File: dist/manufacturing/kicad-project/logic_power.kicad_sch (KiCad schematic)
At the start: 59 parts, among them U22 LMR36510ADDAR, U23 LM66100DCKR, U24 LM66100DCKR, U5 LMR36510ADDAR

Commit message: Complete orderable PD1180-EPR board release
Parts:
- removed GND (x11): GND, symbol Custom:rail_down
- removed USB_VBUS (x2): USB_VBUS, symbol Custom:rail_up
- removed V3V3 (x5): V3V3, symbol Custom:rail_up
- removed V3V3_MOTOR (x5): V3V3_MOTOR, symbol Custom:rail_up
- removed V3V3_USB (x5): V3V3_USB, symbol Custom:rail_up
- removed VMOTOR (x2): VMOTOR, symbol Custom:rail_up
- added GND (x13): GND, symbol Custom:rail_down
- added USB_VBUS (x2): USB_VBUS, symbol Custom:rail_up
- added V3V3 (x4): V3V3, symbol Custom:rail_up
- added V3V3_MOTOR (x5): V3V3_MOTOR, symbol Custom:rail_up
- added V3V3_USB (x6): V3V3_USB, symbol Custom:rail_up
- added VMOTOR (x2): VMOTOR, symbol Custom:rail_up
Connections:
- net GND: now also C15.2, C16.2
- net at C70.1, U24.1 (VIN): now also V3V3_MOTOR.1
- net at C70.2: now also GND.1
- net at C66.1, C67.1: now also V3V3_MOTOR.1; no longer C68.1
- net at C66.2, C67.2: now also GND.1; no longer C68.2
- net at C62.1, C63.1: now also VMOTOR.1
- net at C62.2, C63.2, C64.2: now also GND.1
- net at U23.2 (GND), U23.5 (ST): now also GND.1
- net at R103.2: now also GND.1
- net at U24.2 (GND), U24.5 (ST): now also GND.1
- net at U24.3 (N_CE): now also V3V3.1
- net at U24.6 (VOUT): now also V3V3.1
- net at R17.2: now also GND.1
- net at C69.1: now also V3V3_USB.1; no longer U23.1 (VIN)
- net at C69.2: now also GND.1; no longer C71.2
- net at U23.6 (VOUT): now also C71.1, V3V3.1
- net at C11.2, C12.2, C13.2: now also GND.1
- net at R104.1: now also R102.1, V3V3_MOTOR.1
- net at L1.2: now also V3V3_USB.1
- net at C15.1, C16.1: now also V3V3_USB.1; no longer C17.1
- net at U5.2 (VIN), U5.3 (EN): now also USB_VBUS.1
- net at U23.3 (N_CE): now also V3V3.1
- net at R16.1: now also R18.1, V3V3_USB.1
- net at U22.2 (VIN), U22.3 (EN): now also VMOTOR.1
- net at L2.2: now also V3V3_MOTOR.1
- net at C11.1, C12.1: now also USB_VBUS.1
- new net: C68.1, V3V3_MOTOR.1
- new net: C68.2, GND.1
- new net: C17.1, V3V3_USB.1
- new net: C17.2, GND.1
- new net: C71.2, GND.1
- new net: U23.1 (VIN), V3V3_USB.1
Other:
- note added: "U5: USB 5 V buck. U22: motor-bus auxiliary buck. U23/U24: ideal-diode OR into the shared 3.3 V rail."

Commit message: Fix schematic style and top-side reset switch
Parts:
- removed GND (x13): GND, symbol Custom:rail_down
- removed USB_VBUS (x2): USB_VBUS, symbol Custom:rail_up
- removed V3V3 (x4): V3V3, symbol Custom:rail_up
- removed V3V3_MOTOR (x5): V3V3_MOTOR, symbol Custom:rail_up
- removed V3V3_USB (x6): V3V3_USB, symbol Custom:rail_up
- removed VMOTOR (x2): VMOTOR, symbol Custom:rail_up
- added GND (x14): GND, symbol Custom:rail_down
- added USB_VBUS (x2): USB_VBUS, symbol Custom:rail_up
- added V3V3 (x4): V3V3, symbol Custom:rail_up
- added V3V3_MOTOR (x5): V3V3_MOTOR, symbol Custom:rail_up
- added V3V3_USB (x6): V3V3_USB, symbol Custom:rail_up
- added VMOTOR (x2): VMOTOR, symbol Custom:rail_up
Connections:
- net GND: no longer C15.2, C16.2
- net at U24.2 (GND), U24.5 (ST): now also GND.1
- net at C70.1, U24.1 (VIN): now also V3V3_MOTOR.1
- net at U24.3 (N_CE): now also V3V3.1
- net at U24.6 (VOUT): now also V3V3.1
- net at C66.1, C67.1: now also V3V3_MOTOR.1
- net at R103.2: now also GND.1
- net at U22.2 (VIN), U22.3 (EN): now also VMOTOR.1
- net at C71.1, U23.6 (VOUT): now also V3V3.1
- net at U5.2 (VIN), U5.3 (EN): now also USB_VBUS.1
- net at C68.1: now also V3V3_MOTOR.1
- net at C68.2: now also GND.1
- net at R102.1, R104.1: now also V3V3_MOTOR.1
- net at C11.2, C12.2: now also GND.1; no longer C13.2
- net at C62.1, C63.1: now also VMOTOR.1
- net at C62.2, C63.2: now also GND.1; no longer C64.2
- net at C11.1, C12.1: now also USB_VBUS.1
- net at C69.1: now also V3V3_USB.1
- net at C69.2: now also GND.1
- net at C17.1: now also V3V3_USB.1
- net at C17.2: now also GND.1
- net at C71.2: now also GND.1
- net at L2.2: now also V3V3_MOTOR.1
- net at C15.1, C16.1: now also V3V3_USB.1
- net at R16.1, R18.1: now also V3V3_USB.1
- net at R17.2: now also GND.1
- net at L1.2: now also V3V3_USB.1
- net at U23.1 (VIN): now also V3V3_USB.1
- net at U23.2 (GND), U23.5 (ST): now also GND.1
- net at U23.3 (N_CE): now also V3V3.1
- net at C70.2: now also GND.1
- new net: C64.2, GND.1
- new net: C15.2, C16.2
- new net: C13.2, GND.1

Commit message: Use one USB-C port for PD and data
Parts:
- removed GND (x14): GND, symbol Custom:rail_down
- removed USB_VBUS (x2): USB_VBUS, symbol Custom:rail_up
- removed V3V3 (x4): V3V3, symbol Custom:rail_up
- removed V3V3_MOTOR (x5): V3V3_MOTOR, symbol Custom:rail_up
- removed V3V3_USB (x6): V3V3_USB, symbol Custom:rail_up
- removed VMOTOR (x2): VMOTOR, symbol Custom:rail_up
- added GND (x14): GND, symbol Custom:rail_down
- added USB_VBUS (x2): USB_VBUS, symbol Custom:rail_up
- added V3V3 (x4): V3V3, symbol Custom:rail_up
- added V3V3_MOTOR (x5): V3V3_MOTOR, symbol Custom:rail_up
- added V3V3_USB (x6): V3V3_USB, symbol Custom:rail_up
- added VMOTOR (x2): VMOTOR, symbol Custom:rail_up
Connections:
- net at C68.1: now also V3V3_MOTOR.1
- net at C68.2: now also GND.1
- net at C66.1, C67.1: now also V3V3_MOTOR.1
- net at U23.1 (VIN): now also V3V3_USB.1
- net at R16.1, R18.1: now also V3V3_USB.1
- net at C69.2: now also GND.1
- net at U24.2 (GND), U24.5 (ST): now also GND.1
- net at R102.1, R104.1: now also V3V3_MOTOR.1
- net at C71.1, U23.6 (VOUT): now also V3V3.1
- net at C71.2: now also GND.1
- net at R17.2: now also GND.1
- net at C17.1: now also V3V3_USB.1
- net at C17.2: now also GND.1
- net at U5.2 (VIN), U5.3 (EN): now also USB_VBUS.1
- net at L2.2: now also V3V3_MOTOR.1
- net at C64.2: now also GND.1
- net at C15.1, C16.1: now also V3V3_USB.1
- net at U22.2 (VIN), U22.3 (EN): now also VMOTOR.1
- net at L1.2: now also V3V3_USB.1
- net at C70.1, U24.1 (VIN): now also V3V3_MOTOR.1
- net at C70.2: now also GND.1
- net at R103.2: now also GND.1
- net at U23.2 (GND), U23.5 (ST): now also GND.1
- net at U23.3 (N_CE): now also V3V3.1
- net at C11.1, C12.1: now also USB_VBUS.1
- net at C11.2, C12.2: now also GND.1
- net at U24.6 (VOUT): now also V3V3.1
- net at C62.1, C63.1: now also VMOTOR.1
- net at C62.2, C63.2: now also GND.1
- net at C69.1: now also V3V3_USB.1
- net at U24.3 (N_CE): now also V3V3.1
- net at C13.2: now also GND.1

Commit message: fix: finalize single-port EPR controller
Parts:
- removed GND (x14): GND, symbol Custom:rail_down
- removed USB_VBUS (x2): USB_VBUS, symbol Custom:rail_up
- removed V3V3 (x4): V3V3, symbol Custom:rail_up
- removed V3V3_MOTOR (x5): V3V3_MOTOR, symbol Custom:rail_up
- removed V3V3_USB (x6): V3V3_USB, symbol Custom:rail_up
- removed VMOTOR (x2): VMOTOR, symbol Custom:rail_up
- added R111: 10kΩ, resistor_res0603, symbol Device:boxresistor_down
- C11, C62: footprint (none) -> capacitor_cap1206
- C12, C13, C14, C63, C64, C65, C69, C70, C71: footprint (none) -> capacitor_cap0603
- C15, C16, C17, C66, C67, C68: footprint (none) -> capacitor_cap0805
- L1, L2: footprint (none) -> SWPA6045S220MT
- R102, R103, R104, R16, R17, R18: footprint (none) -> resistor_res0603
- U22, U5: footprint (none) -> LMR36510ADDAR
- U23, U24: footprint (none) -> LM66100DCKR
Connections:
- net GND: now also C11.2, C12.2, C13.2, C15.2, C16.2, C17.2, C62.2, C63.2, C64.2, C66.2, C67.2, C68.2, C69.2, C70.2, C71.2, R103.2, R17.2, U23.2 (GND), U24.2 (GND), U24.5 (ST), U5.1 (PGND), U5.9 (PAD)
- net BUCK_SW: now reaches L1.1
- net BUCK_SW: now also C14.2, U5.8 (SW)
- net V3V3_USB: now reaches L1.2
- net V3V3_USB: now also C15.1, C16.1, C17.1, C69.1, R16.1, R18.1, U23.1 (VIN), R111.1
- net V3V3_MOTOR: now reaches R102.1, R104.1
- net V3V3_MOTOR: now also C66.1, C67.1, C68.1, C70.1, L2.2, U23.3 (N_CE), U24.1 (VIN)
- net MOTOR_BUCK_FB: now reaches R102.2, R103.1
- net MOTOR_BUCK_FB: now also U22.5 (FB)
- net BUCK_VCC: now reaches C13.1
- net BUCK_VCC: now also U5.6 (VCC)
- net VMOTOR: now reaches C62.1, C63.1
- net VMOTOR: now also U22.2 (VIN), U22.3 (EN)
- net USB_VBUS: now reaches U5.2 (VIN), U5.3 (EN)
- net USB_VBUS: now also C11.1, C12.1
- net BUCK_FB: now reaches R16.2, R17.1
- net BUCK_FB: now also U5.5 (FB)
- net MOTOR_BUCK_SW: now reaches L2.1
- net MOTOR_BUCK_SW: now also C65.2, U22.8 (SW)
- net MOTOR_LOGIC_PG: now reaches U22.4 (PG)
- net MOTOR_LOGIC_PG: now also R104.2
- net MOTOR_BUCK_VCC: now reaches U22.6 (VCC)
- net MOTOR_BUCK_VCC: now also C64.1
- net MOTOR_BUCK_BOOT: now reaches U22.7 (BOOT)
- net MOTOR_BUCK_BOOT: now also C65.1
- net V3V3: now reaches C71.1, U23.6 (VOUT)
- net V3V3: now also U24.6 (VOUT)
- net LOGIC_OR_PRIORITY: now reaches U24.3 (N_CE)
- net LOGIC_OR_PRIORITY: now also U23.5 (ST), R111.2
- net LOGIC_PG: now reaches R18.2
- net LOGIC_PG: now also U5.4 (PG)
- net BUCK_BOOT: now reaches U5.7 (BOOT)
- net BUCK_BOOT: now also C14.1
- no-connect marks 0 -> 2
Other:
- note added: "LOGIC_OR_PRIORITY"
- note added: "U5: USB 5 V buck. U22: motor-bus auxiliary buck. U23/U24 + R111: status-interlocked ideal-diode OR into the shared 3.3 V rail."
- note removed: "U5: USB 5 V buck. U22: motor-bus auxiliary buck. U23/U24: ideal-diode OR into the shared 3.3 V rail."

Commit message: Implement dual USB power/data ECO and consolidate industrial I/O
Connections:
- net USB_VBUS renamed PD_VBUS
- net V3V3_USB renamed V3V3_PD
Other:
- note added: "02 / PD and Motor Backup Supplies"
- note added: "PD VBUS starts the 3.3 V rail; the motor-bus buck retains brake-control backup after PD loss."
- note added: "U5: PD 5-48 V buck. U22: VMOTOR backup buck. U23/U24 + R111: status-interlocked ideal-diode OR into the shared 3.3 V rail."
- note removed: "02 / USB and Motor Logic Supplies"
- note removed: "Either USB or motor bus sustains 3.3 V; ideal diodes block reverse current."
- note removed: "U5: USB 5 V buck. U22: motor-bus auxiliary buck. U23/U24 + R111: status-interlocked ideal-diode OR into the shared 3.3 V rail."

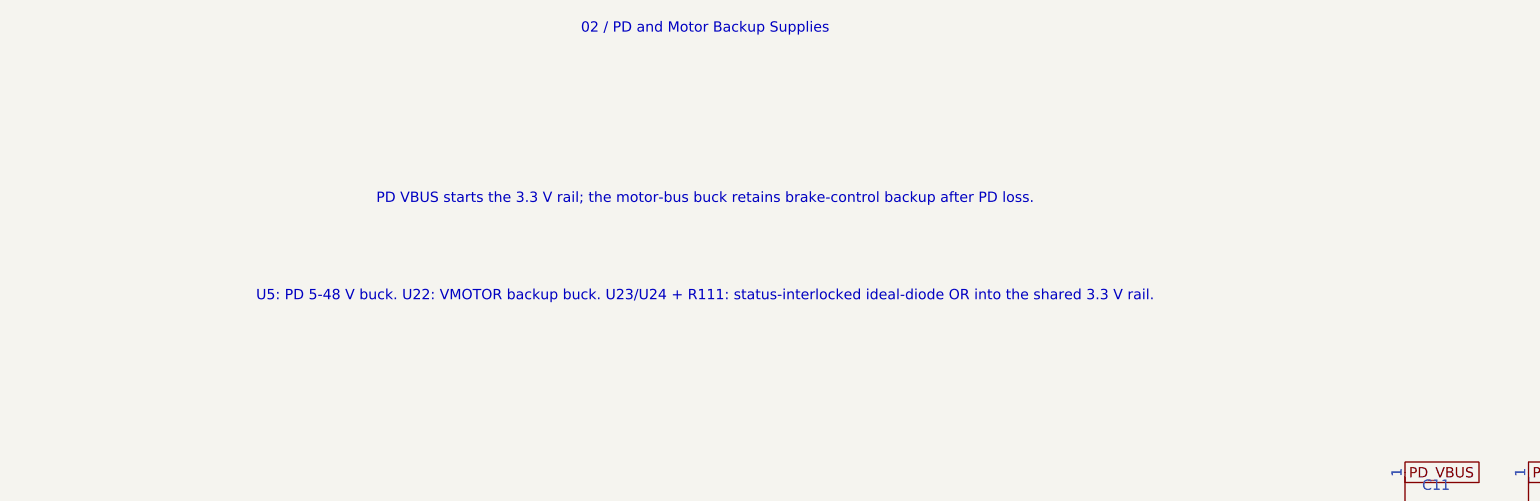
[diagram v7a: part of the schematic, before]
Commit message: Complete top-side routing and verify reference-board ECO
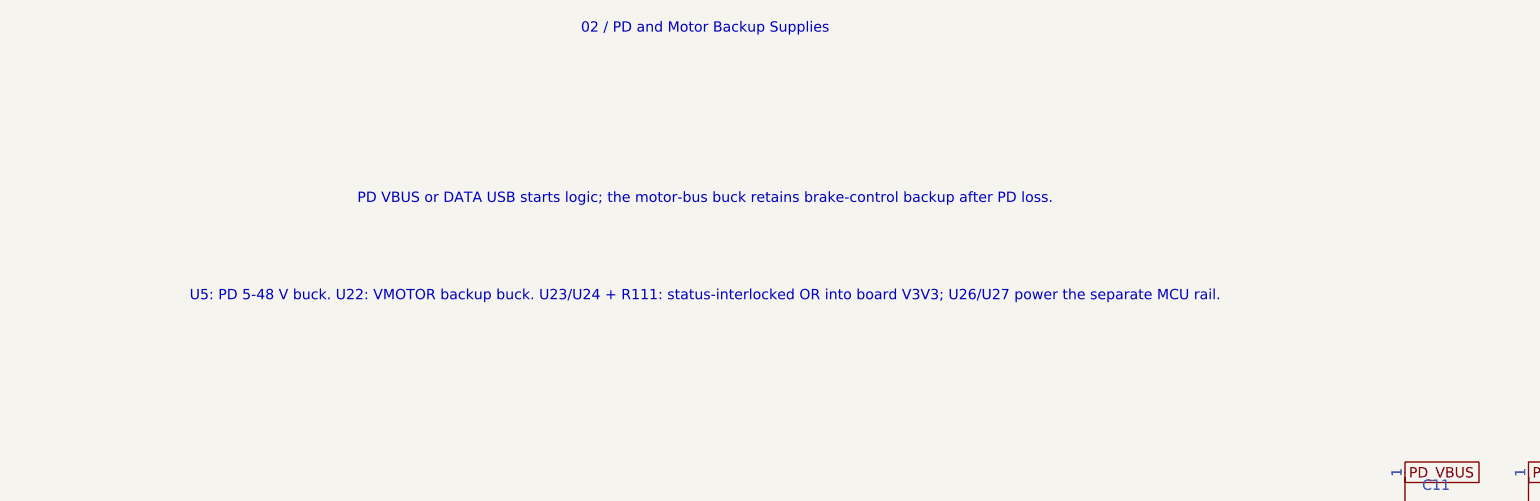
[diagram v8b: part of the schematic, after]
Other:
- note added: "PD VBUS or DATA USB starts logic; the motor-bus buck retains brake-control backup after PD loss."
- note added: "U5: PD 5-48 V buck. U22: VMOTOR backup buck. U23/U24 + R111: status-interlocked OR into board V3V3; U26/U27 power the separate MCU rail."
- note removed: "PD VBUS starts the 3.3 V rail; the motor-bus buck retains brake-control backup after PD loss."
- note removed: "U5: PD 5-48 V buck. U22: VMOTOR backup buck. U23/U24 + R111: status-interlocked ideal-diode OR into the shared 3.3 V rail."
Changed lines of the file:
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@@
     (instances
       (project ""
-        (path "/4ef2daa1-40fc-426a-abb2-c834ba40a3c9/5821f0f1-72ca-4170-b960-aa78edeb1140"
+        (path "/953e0ace-4c89-4879-a4e2-9aa73ffc3208/8c82c75e-0be6-418f-b9c6-458c3db933a1"
           (reference "U5")
           (unit 1)
@@
     (instances
       (project ""
-        (path "/4ef2daa1-40fc-426a-abb2-c834ba40a3c9/5821f0f1-72ca-4170-b960-aa78edeb1140"
+        (path "/953e0ace-4c89-4879-a4e2-9aa73ffc3208/8c82c75e-0be6-418f-b9c6-458c3db933a1"
           (reference "L1")
           (unit 1)
@@
     (instances
       (project ""
-        (path "/4ef2daa1-40fc-426a-abb2-c834ba40a3c9/5821f0f1-72ca-4170-b960-aa78edeb1140"
+        (path "/953e0ace-4c89-4879-a4e2-9aa73ffc3208/8c82c75e-0be6-418f-b9c6-458c3db933a1"
           (reference "C11")
           (unit 1)
@@
     (instances
       (project ""
-        (path "/4ef2daa1-40fc-426a-abb2-c834ba40a3c9/5821f0f1-72ca-4170-b960-aa78edeb1140"
+        (path "/953e0ace-4c89-4879-a4e2-9aa73ffc3208/8c82c75e-0be6-418f-b9c6-458c3db933a1"
           (reference "C12")
           (unit 1)
@@
     (instances
       (project ""
-        (path "/4ef2daa1-40fc-426a-abb2-c834ba40a3c9/5821f0f1-72ca-4170-b960-aa78edeb1140"
+        (path "/953e0ace-4c89-4879-a4e2-9aa73ffc3208/8c82c75e-0be6-418f-b9c6-458c3db933a1"
           (reference "C13")
           (unit 1)
@@
     (instances
       (project ""
-        (path "/4ef2daa1-40fc-426a-abb2-c834ba40a3c9/5821f0f1-72ca-4170-b960-aa78edeb1140"
+        (path "/953e0ace-4c89-4879-a4e2-9aa73ffc3208/8c82c75e-0be6-418f-b9c6-458c3db933a1"
           (reference "C14")
           (unit 1)
@@
     (instances
       (project ""
-        (path "/4ef2daa1-40fc-426a-abb2-c834ba40a3c9/5821f0f1-72ca-4170-b960-aa78edeb1140"
+        (path "/953e0ace-4c89-4879-a4e2-9aa73ffc3208/8c82c75e-0be6-418f-b9c6-458c3db933a1"
           (reference "C15")
           (unit 1)
@@
     (instances
       (project ""
-        (path "/4ef2daa1-40fc-426a-abb2-c834ba40a3c9/5821f0f1-72ca-4170-b960-aa78edeb1140"
+        (path "/953e0ace-4c89-4879-a4e2-9aa73ffc3208/8c82c75e-0be6-418f-b9c6-458c3db933a1"
           (reference "C16")
           (unit 1)
@@
     (instances
       (project ""
-        (path "/4ef2daa1-40fc-426a-abb2-c834ba40a3c9/5821f0f1-72ca-4170-b960-aa78edeb1140"
+        (path "/953e0ace-4c89-4879-a4e2-9aa73ffc3208/8c82c75e-0be6-418f-b9c6-458c3db933a1"
           (reference "C17")
           (unit 1)
@@
     (instances
       (project ""
-        (path "/4ef2daa1-40fc-426a-abb2-c834ba40a3c9/5821f0f1-72ca-4170-b960-aa78edeb1140"
+        (path "/953e0ace-4c89-4879-a4e2-9aa73ffc3208/8c82c75e-0be6-418f-b9c6-458c3db933a1"
           (reference "R16")
           (unit 1)
@@
     (instances
       (project ""
-        (path "/4ef2daa1-40fc-426a-abb2-c834ba40a3c9/5821f0f1-72ca-4170-b960-aa78edeb1140"
+        (path "/953e0ace-4c89-4879-a4e2-9aa73ffc3208/8c82c75e-0be6-418f-b9c6-458c3db933a1"
           (reference "R17")
           (unit 1)
@@
     (instances
       (project ""
-        (path "/4ef2daa1-40fc-426a-abb2-c834ba40a3c9/5821f0f1-72ca-4170-b960-aa78edeb1140"
+        (path "/953e0ace-4c89-4879-a4e2-9aa73ffc3208/8c82c75e-0be6-418f-b9c6-458c3db933a1"
           (reference "R18")
           (unit 1)
@@
     (instances
       (project ""
-        (path "/4ef2daa1-40fc-426a-abb2-c834ba40a3c9/5821f0f1-72ca-4170-b960-aa78edeb1140"
+        (path "/953e0ace-4c89-4879-a4e2-9aa73ffc3208/8c82c75e-0be6-418f-b9c6-458c3db933a1"
           (reference "U22")
           (unit 1)
@@
     (instances
       (project ""
-        (path "/4ef2daa1-40fc-426a-abb2-c834ba40a3c9/5821f0f1-72ca-4170-b960-aa78edeb1140"
+        (path "/953e0ace-4c89-4879-a4e2-9aa73ffc3208/8c82c75e-0be6-418f-b9c6-458c3db933a1"
           (reference "L2")
           (unit 1)
@@
     (instances
       (project ""
-        (path "/4ef2daa1-40fc-426a-abb2-c834ba40a3c9/5821f0f1-72ca-4170-b960-aa78edeb1140"
+        (path "/953e0ace-4c89-4879-a4e2-9aa73ffc3208/8c82c75e-0be6-418f-b9c6-458c3db933a1"
           (reference "C62")
           (unit 1)
@@
     (instances
       (project ""
-        (path "/4ef2daa1-40fc-426a-abb2-c834ba40a3c9/5821f0f1-72ca-4170-b960-aa78edeb1140"
+        (path "/953e0ace-4c89-4879-a4e2-9aa73ffc3208/8c82c75e-0be6-418f-b9c6-458c3db933a1"
           (reference "C63")
           (unit 1)
@@
     (instances
       (project ""
-        (path "/4ef2daa1-40fc-426a-abb2-c834ba40a3c9/5821f0f1-72ca-4170-b960-aa78edeb1140"
+        (path "/953e0ace-4c89-4879-a4e2-9aa73ffc3208/8c82c75e-0be6-418f-b9c6-458c3db933a1"
           (reference "C64")
           (unit 1)
@@
     (instances
       (project ""
-        (path "/4ef2daa1-40fc-426a-abb2-c834ba40a3c9/5821f0f1-72ca-4170-b960-aa78edeb1140"
+        (path "/953e0ace-4c89-4879-a4e2-9aa73ffc3208/8c82c75e-0be6-418f-b9c6-458c3db933a1"
           (reference "C65")
           (unit 1)
@@
     (instances
       (project ""
-        (path "/4ef2daa1-40fc-426a-abb2-c834ba40a3c9/5821f0f1-72ca-4170-b960-aa78edeb1140"
+        (path "/953e0ace-4c89-4879-a4e2-9aa73ffc3208/8c82c75e-0be6-418f-b9c6-458c3db933a1"
           (reference "C66")
           (unit 1)
@@
     (instances
       (project ""
-        (path "/4ef2daa1-40fc-426a-abb2-c834ba40a3c9/5821f0f1-72ca-4170-b960-aa78edeb1140"
+        (path "/953e0ace-4c89-4879-a4e2-9aa73ffc3208/8c82c75e-0be6-418f-b9c6-458c3db933a1"
           (reference "C67")
           (unit 1)
@@
     (instances
       (project ""
-        (path "/4ef2daa1-40fc-426a-abb2-c834ba40a3c9/5821f0f1-72ca-4170-b960-aa78edeb1140"
+        (path "/953e0ace-4c89-4879-a4e2-9aa73ffc3208/8c82c75e-0be6-418f-b9c6-458c3db933a1"
           (reference "C68")
           (unit 1)
@@
     (instances
       (project ""
-        (path "/4ef2daa1-40fc-426a-abb2-c834ba40a3c9/5821f0f1-72ca-4170-b960-aa78edeb1140"
+        (path "/953e0ace-4c89-4879-a4e2-9aa73ffc3208/8c82c75e-0be6-418f-b9c6-458c3db933a1"
           (reference "R102")
           (unit 1)
@@
     (instances
       (project ""
-        (path "/4ef2daa1-40fc-426a-abb2-c834ba40a3c9/5821f0f1-72ca-4170-b960-aa78edeb1140"
+        (path "/953e0ace-4c89-4879-a4e2-9aa73ffc3208/8c82c75e-0be6-418f-b9c6-458c3db933a1"
           (reference "R103")
           (unit 1)
@@
     (instances
       (project ""
-        (path "/4ef2daa1-40fc-426a-abb2-c834ba40a3c9/5821f0f1-72ca-4170-b960-aa78edeb1140"
+        (path "/953e0ace-4c89-4879-a4e2-9aa73ffc3208/8c82c75e-0be6-418f-b9c6-458c3db933a1"
           (reference "R104")
           (unit 1)
@@
     (instances
       (project ""
-        (path "/4ef2daa1-40fc-426a-abb2-c834ba40a3c9/5821f0f1-72ca-4170-b960-aa78edeb1140"
+        (path "/953e0ace-4c89-4879-a4e2-9aa73ffc3208/8c82c75e-0be6-418f-b9c6-458c3db933a1"
           (reference "U23")
           (unit 1)
@@
     (instances
       (project ""
-        (path "/4ef2daa1-40fc-426a-abb2-c834ba40a3c9/5821f0f1-72ca-4170-b960-aa78edeb1140"
+        (path "/953e0ace-4c89-4879-a4e2-9aa73ffc3208/8c82c75e-0be6-418f-b9c6-458c3db933a1"
           (reference "U24")
           (unit 1)
@@
     (instances
       (project ""
-        (path "/4ef2daa1-40fc-426a-abb2-c834ba40a3c9/5821f0f1-72ca-4170-b960-aa78edeb1140"
+        (path "/953e0ace-4c89-4879-a4e2-9aa73ffc3208/8c82c75e-0be6-418f-b9c6-458c3db933a1"
           (reference "R111")
           (unit 1)
@@
     (instances
       (project ""
-        (path "/4ef2daa1-40fc-426a-abb2-c834ba40a3c9/5821f0f1-72ca-4170-b960-aa78edeb1140"
+        (path "/953e0ace-4c89-4879-a4e2-9aa73ffc3208/8c82c75e-0be6-418f-b9c6-458c3db933a1"
           (reference "C69")
           (unit 1)
@@
     (instances
       (project ""
-        (path "/4ef2daa1-40fc-426a-abb2-c834ba40a3c9/5821f0f1-72ca-4170-b960-aa78edeb1140"
+        (path "/953e0ace-4c89-4879-a4e2-9aa73ffc3208/8c82c75e-0be6-418f-b9c6-458c3db933a1"
           (reference "C70")
           (unit 1)
@@
     (instances
       (project ""
-        (path "/4ef2daa1-40fc-426a-abb2-c834ba40a3c9/5821f0f1-72ca-4170-b960-aa78edeb1140"
+        (path "/953e0ace-4c89-4879-a4e2-9aa73ffc3208/8c82c75e-0be6-418f-b9c6-458c3db933a1"
           (reference "C71")
           (unit 1)
@@
     )
   )
-  (text "PD VBUS starts the 3.3 V rail; the motor-bus buck retains brake-control backup after PD loss."
+  (text "PD VBUS or DATA USB starts logic; the motor-bus buck retains brake-control backup after PD loss."
     (at 285.8 60.30000000000001 0)
     (effects
@@
     )
   )
-  (text "U5: PD 5-48 V buck. U22: VMOTOR backup buck. U23/U24 + R111: status-interlocked ideal-diode OR into the shared 3.3 V rail."
+  (text "U5: PD 5-48 V buck. U22: VMOTOR backup buck. U23/U24 + R111: status-interlocked OR into board V3V3; U26/U27 power the separate MCU rail."
     (at 285.8 72.30000000000001 0)
     (effects
